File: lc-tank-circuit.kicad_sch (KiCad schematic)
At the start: 12 parts, among them Q2 2N3904, Q3 IRF9540N

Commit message: Update kicad to rev 0.1
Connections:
- net PWM_TUNING renamed PWM_TUNING_INPUT
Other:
- note added: "En NPN-Transistor som styr en P-Kanals MOSFET, Duty Cycle avgör backspänning till varaktorernas katoder för att bestämma kapacitansen i LC-kretsen PWM_TUNING_INPUT:s Duty Cycle orsakar att MOSFET stänger och öppnar t.ex. 50% av tiden då får vi spänningen 4.5V (RC-filter jämnar ut)"
- note added: "PWM-Styrsignal"
- note added: "RC filter Fc = 16 Hz"
- note removed: "RC filter"
- moved on the sheet: C6, C8, C9, D3, D4, L1, Q2, Q3, R1, R17, R3, R5

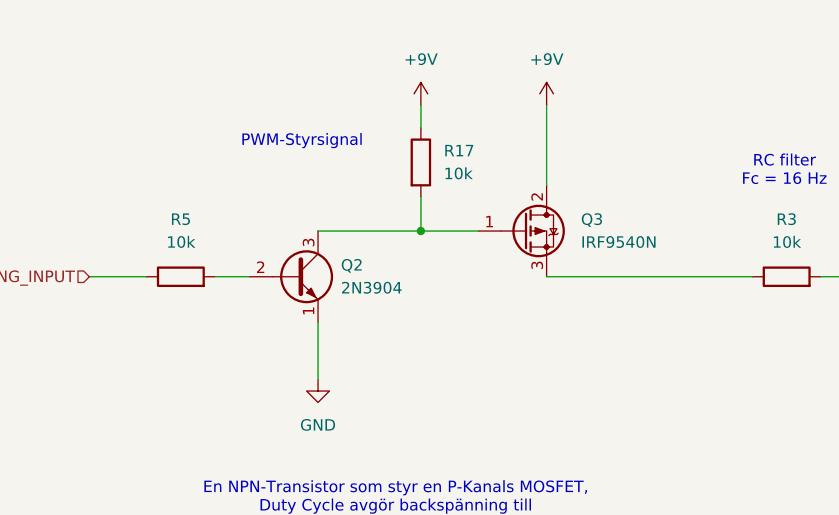
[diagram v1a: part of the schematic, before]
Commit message: Add PWM-code on Timer2/PB3
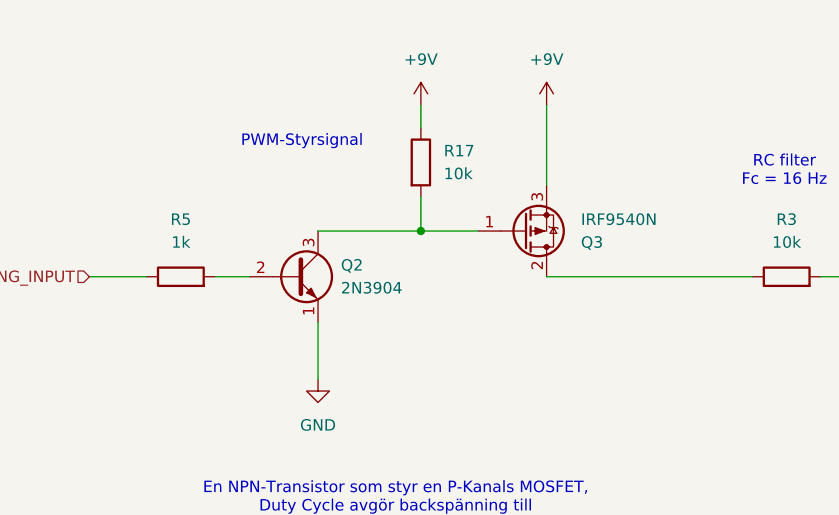
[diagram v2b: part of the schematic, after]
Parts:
- R5: value 10k -> 1k
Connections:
- net +9V: now also Q3.3 (S); no longer Q3.2 (D)
- net at R3.1: now also Q3.2 (D); no longer Q3.3 (S)
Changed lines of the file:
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@@
 			)
 		)
-		(property "Value" "10k"
+		(property "Value" "1k"
 			(at 62.23 86.36 90)
 			(effects
@@
 		(lib_id "Transistor_FET:IRF9540N")
 		(at 100.33 85.09 0)
+		(mirror x)
 		(unit 1)
 		(exclude_from_sim no)
@@
 		(on_board yes)
 		(dnp no)
-		(fields_autoplaced yes)
 		(property "Reference" "Q3"
-			(at 106.68 83.8199 0)
+			(at 106.68 86.3601 0)
 			(effects
 				(font
@@
 		)
 		(property "Value" "IRF9540N"
-			(at 106.68 86.3599 0)
+			(at 106.68 83.8201 0)
 			(effects
 				(font
@@
 		)
 		(property "Footprint" "Package_TO_SOT_THT:TO-220-3_Vertical"
-			(at 105.41 86.995 0)
+			(at 105.41 83.185 0)
 			(effects
 				(font
@@
 		)
 		(property "Datasheet" "http://www.irf.com/product-info/datasheets/data/irf9540n.pdf"
-			(at 105.41 88.9 0)
+			(at 105.41 81.28 0)
 			(effects
 				(font
@@
 			)
 		)
-		(pin "1"
-		)
 		(pin "3"
 		)
 		(pin "2"
 		)
+		(pin "1"
+		)
 		(instances
